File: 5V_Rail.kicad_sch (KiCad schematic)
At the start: 43 parts

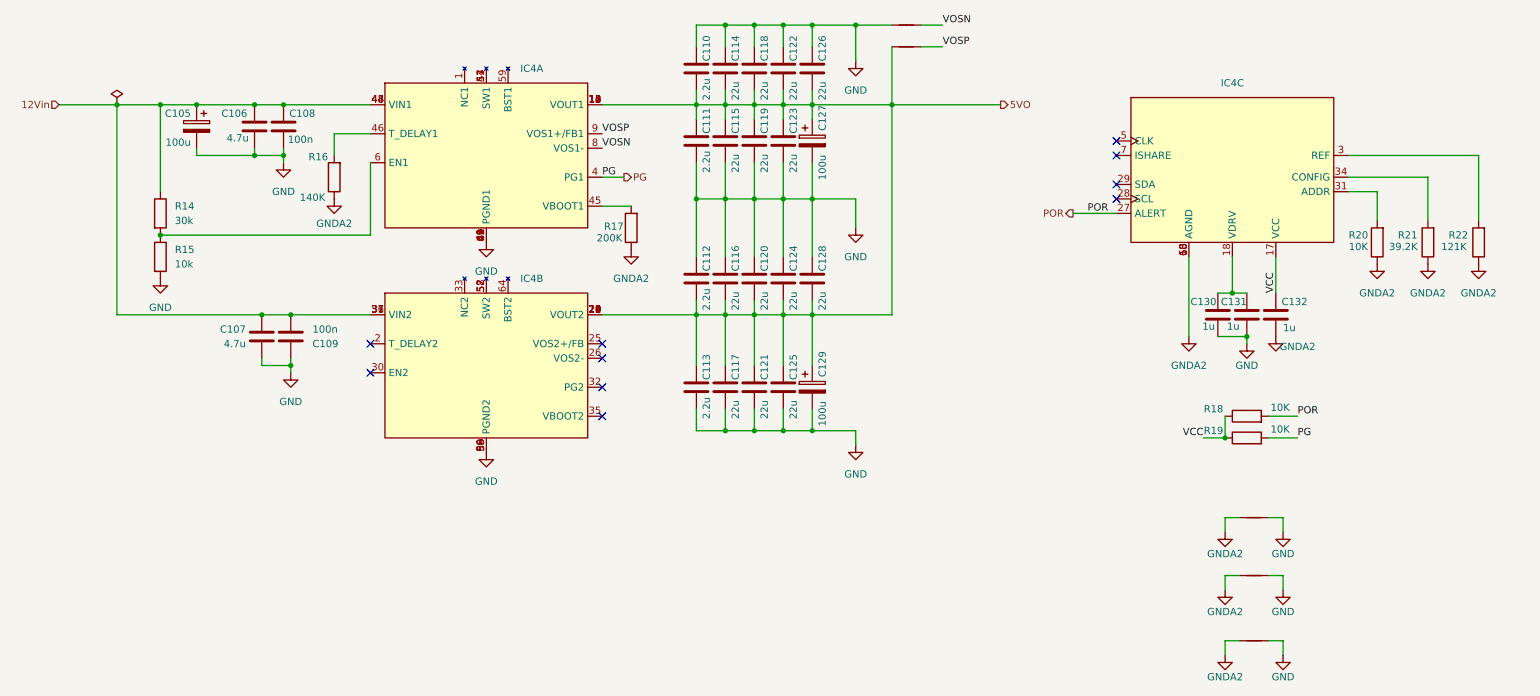
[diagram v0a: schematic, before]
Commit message: <feat>: Modified Power Tree
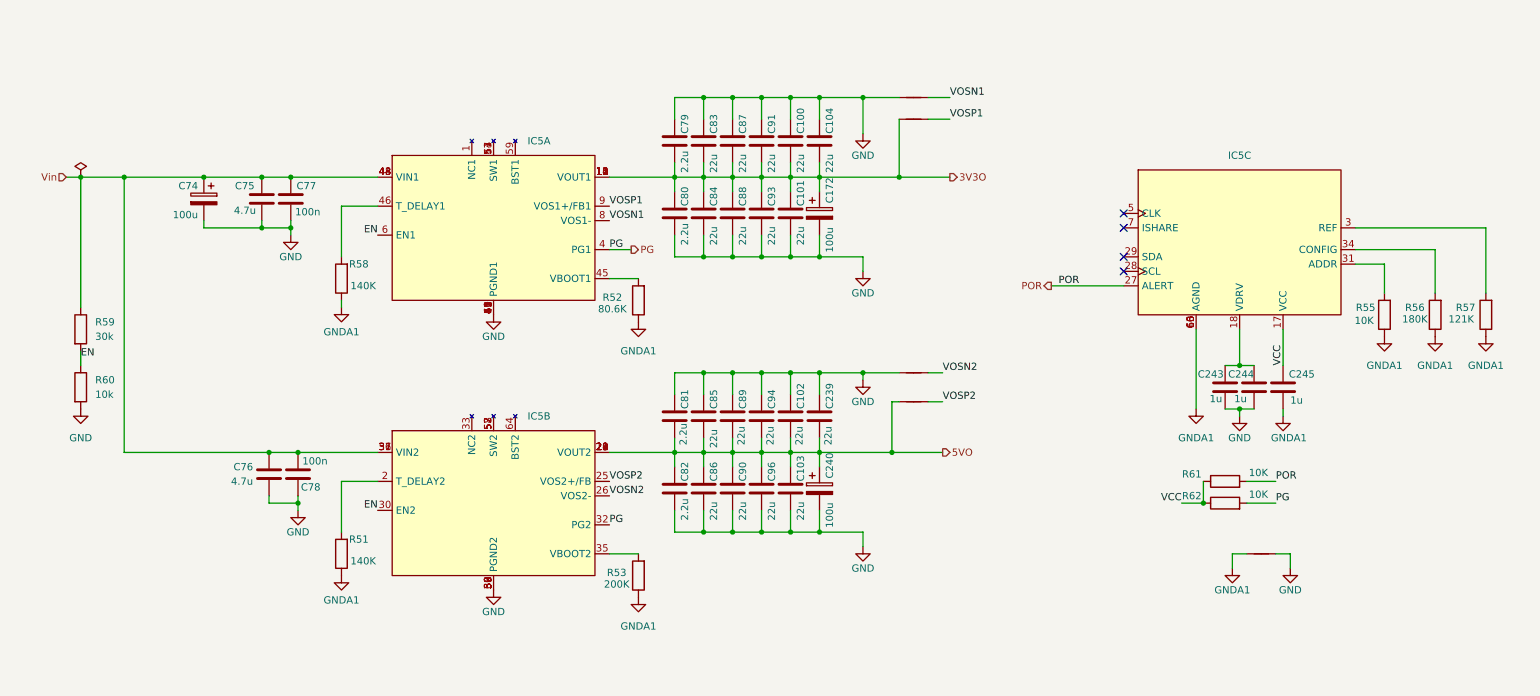
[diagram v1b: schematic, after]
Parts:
- removed C105, C127, C129: 100u, Capacitor_Tantalum_SMD:CP_EIA-7343-20_Kemet-V, symbol Device:C_Polarized
- removed C106, C107: 4.7u, Capacitor_SMD:C_0603_1608Metric, symbol Device:C
- removed C108, C109: 100n, Capacitor_SMD:C_0603_1608Metric, symbol Device:C
- removed C110, C111, C112, C113: 2.2u, Capacitor_SMD:C_0805_2012Metric, symbol Device:C
- removed C114, C115, C116, C117, C118, C119, C120, C121, C122, C123, C124, C125, C126, C128: 22u, Capacitor_SMD:C_1206_3216Metric, symbol Device:C
- removed C130, C131, C132: 1u, Capacitor_SMD:C_0402_1005Metric, symbol Device:C
- removed IC4: (no value), dfdtc_DCDC:NDE12D15R-S, symbol dfdtc_DCDC_Module:NDE12D15R-S
- removed NT12, NT13, NT14, NT15, NT16: NetTie_2, NetTie:NetTie-2_SMD_Pad0.5mm, symbol Device:NetTie_2
- removed R14: 30k, Resistor_SMD:R_0201_0603Metric, symbol Device:R
- removed R15: 10k, Resistor_SMD:R_0201_0603Metric, symbol Device:R
- removed R16: 140K, Resistor_SMD:R_0201_0603Metric, symbol Device:R
- removed R17: 200K, Resistor_SMD:R_0201_0603Metric, symbol Device:R
- removed R18, R19, R20: 10K, Resistor_SMD:R_0201_0603Metric, symbol Device:R
- removed R21: 39.2K, Resistor_SMD:R_0201_0603Metric, symbol Device:R
- removed R22: 121K, Resistor_SMD:R_0201_0603Metric, symbol Device:R
- added C100, C101, C102, C103, C104, C239, C83, C84, C85, C86, C87, C88, C89, C90, C91, C93, C94, C96: 22u, Capacitor_SMD:C_1206_3216Metric, symbol Device:C
- added C172, C240, C74: 100u, Capacitor_Tantalum_SMD:CP_EIA-7343-20_Kemet-V, symbol Device:C_Polarized
- added C243, C244, C245: 1u, Capacitor_SMD:C_0402_1005Metric, symbol Device:C
- added C75, C76: 4.7u, Capacitor_SMD:C_0603_1608Metric, symbol Device:C
- added C77, C78: 100n, Capacitor_SMD:C_0603_1608Metric, symbol Device:C
- added C79, C80, C81, C82: 2.2u, Capacitor_SMD:C_0805_2012Metric, symbol Device:C
- added IC5: (no value), dfdtc_DCDC:NDE12D15R-S, symbol dfdtc_DCDC_Module:NDE12D15R-S
- added NT17, NT18, NT19, NT20, NT21: NetTie_2, NetTie:NetTie-2_SMD_Pad0.5mm, symbol Device:NetTie_2
- added R51, R58: 140K, Resistor_SMD:R_0201_0603Metric, symbol Device:R
- added R52: 80.6K, Resistor_SMD:R_0201_0603Metric, symbol Device:R
- added R53: 200K, Resistor_SMD:R_0201_0603Metric, symbol Device:R
- added R55, R61, R62: 10K, Resistor_SMD:R_0201_0603Metric, symbol Device:R
- added R56: 180K, Resistor_SMD:R_0201_0603Metric, symbol Device:R
- added R57: 121K, Resistor_SMD:R_0201_0603Metric, symbol Device:R
- added R59: 30k, Resistor_SMD:R_0201_0603Metric, symbol Device:R
- added R60: 10k, Resistor_SMD:R_0201_0603Metric, symbol Device:R
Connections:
- net 5VO: now also C102.2, C103.1, C239.2, C240.1, C81.2, C82.1, C85.2, C86.1, C89.2, C90.1, C94.2, C96.1, IC5.19 (VOUT2), IC5.20 (VOUT2), IC5.21 (VOUT2), IC5.22 (VOUT2), IC5.23 (VOUT2), IC5.24 (VOUT2), NT20.1
- net GND: now also C100.1, C101.2, C102.1, C103.2, C104.1, C172.2, C239.1, C240.2, C243.2, C244.2, C74.2, C75.2, C76.2, C77.2, C78.1, C79.1, C80.2, C81.1, C82.2, C83.1, C84.2, C85.1, C86.2, C87.1, C88.2, C89.1, C90.2, C91.1, C93.2, C94.1, C96.2, IC5.38 (PGND2), IC5.39 (PGND2), IC5.40 (PGND1), IC5.41 (PGND1), IC5.42 (PGND1), IC5.49 (PGND1), IC5.50 (PGND2), IC5.55 (PGND1), IC5.56 (PGND2), IC5.61 (PGND1), IC5.62 (PGND2), NT17.1, NT19.1, NT21.2, R60.2
- net PG: now also IC5.32 (PG2), IC5.4 (PG1), R62.2
- net POR: now also IC5.27 (ALERT), R61.2
- net VCC: now also C245.1, IC5.17 (VCC), R61.1, R62.1
- new net: IC5.35 (VBOOT2), R53.2
- new net: C243.1, C244.1, IC5.18 (VDRV)
- new net: IC5.45 (VBOOT1), R52.2
- new net: IC5.46 (T_DELAY1), R58.2
- new net: IC5.47 (SW1), IC5.53 (SW1), IC5.54 (SW1)
- new net: IC5.3 (REF), R57.2
- new net: IC5.31 (ADDR), R55.2
- new net: IC5.34 (CONFIG), R56.2
- new net: IC5.2 (T_DELAY2), R51.2
- new net: IC5.52 (SW2), IC5.57 (SW2), IC5.58 (SW2)
- new net 3V3O: C100.2, C101.1, C104.2, C172.1, C79.2, C80.1, C83.2, C84.1, C87.2, C88.1, C91.2, C93.1, IC5.10 (VOUT1), IC5.11 (VOUT1), IC5.12 (VOUT1), IC5.13 (VOUT1), IC5.14 (VOUT1), IC5.15 (VOUT1), NT18.1
- new net EN: IC5.30 (EN2), IC5.6 (EN1), R59.2, R60.1
- new net GNDA1: C245.2, IC5.16 (AGND), IC5.60 (AGND), IC5.63 (AGND), NT21.1, R51.1, R52.1, R53.1, R55.1, R56.1, R57.1, R58.1
- new net VOSN1: IC5.8 (VOS1-), NT17.2
- new net VOSN2: IC5.26 (VOS2-), NT19.2
- new net VOSP1: IC5.9 (VOS1+/FB1), NT18.2
- new net VOSP2: IC5.25 (VOS2+/FB), NT20.2
- new net Vin: C74.1, C75.1, C76.1, C77.1, C78.2, IC5.36 (VIN2), IC5.37 (VIN2), IC5.43 (VIN1), IC5.44 (VIN1), IC5.48 (VIN1), IC5.51 (VIN2), R59.1
- no-connect marks 10 -> 4

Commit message: sync works
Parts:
- removed C100, C101, C102, C103, C104, C239, C91, C93, C94, C96: 22u, Capacitor_SMD:C_1206_3216Metric, symbol Device:C
- removed C172, C240: 100u, Capacitor_Tantalum_SMD:CP_EIA-7343-20_Kemet-V, symbol Device:C_Polarized
- removed NT17, NT18, NT19, NT20: NetTie_2, NetTie:NetTie-2_SMD_Pad0.5mm, symbol Device:NetTie_2
- removed R51: 140K, Resistor_SMD:R_0201_0603Metric, symbol Device:R
- removed R53: 200K, Resistor_SMD:R_0201_0603Metric, symbol Device:R
- C83, C84, C85, C86, C87, C88, C89, C90: value 22u -> 100u
- R56: value 180K -> 39.2K
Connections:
- net 5VO is gone; now on net 3V3O: C81.2, C82.1, C85.2, C86.1, C89.2, C90.1, IC5.19 (VOUT2), IC5.20 (VOUT2), IC5.21 (VOUT2), IC5.22 (VOUT2), IC5.23 (VOUT2), IC5.24 (VOUT2)
- net VOSN1 is gone; now on net GND: IC5.8 (VOS1-)
- net VOSP1 is gone; now on net 3V3O: IC5.9 (VOS1+/FB1)
- net EN: no longer IC5.30 (EN2)
- net GND: now also C245.2
- net GNDA1: no longer C245.2
- net PG: no longer IC5.32 (PG2)
- net VOSN2: no longer names the net of IC5.26 (VOS2-)
- net VOSP2: no longer names the net of IC5.25 (VOS2+/FB)
- no-connect marks 4 -> 10
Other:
- moved on the sheet: C243, C244, C245, C74, C75, C76, C77, C78, C79, C80, C81, C82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
